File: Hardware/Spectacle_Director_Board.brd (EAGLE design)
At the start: 25.4 x 55.9 mm, 69 parts, among them J1 AUDIO-JACK3, J4 AUDIO-JACK3, Q2 MBT3904DW1T1, U1 CY7C65213, U2 ESP3212, U3 AP2112K-3.3V, U5 W25Q32FVSS, Y1 26MHz, Y2 32.768kHz

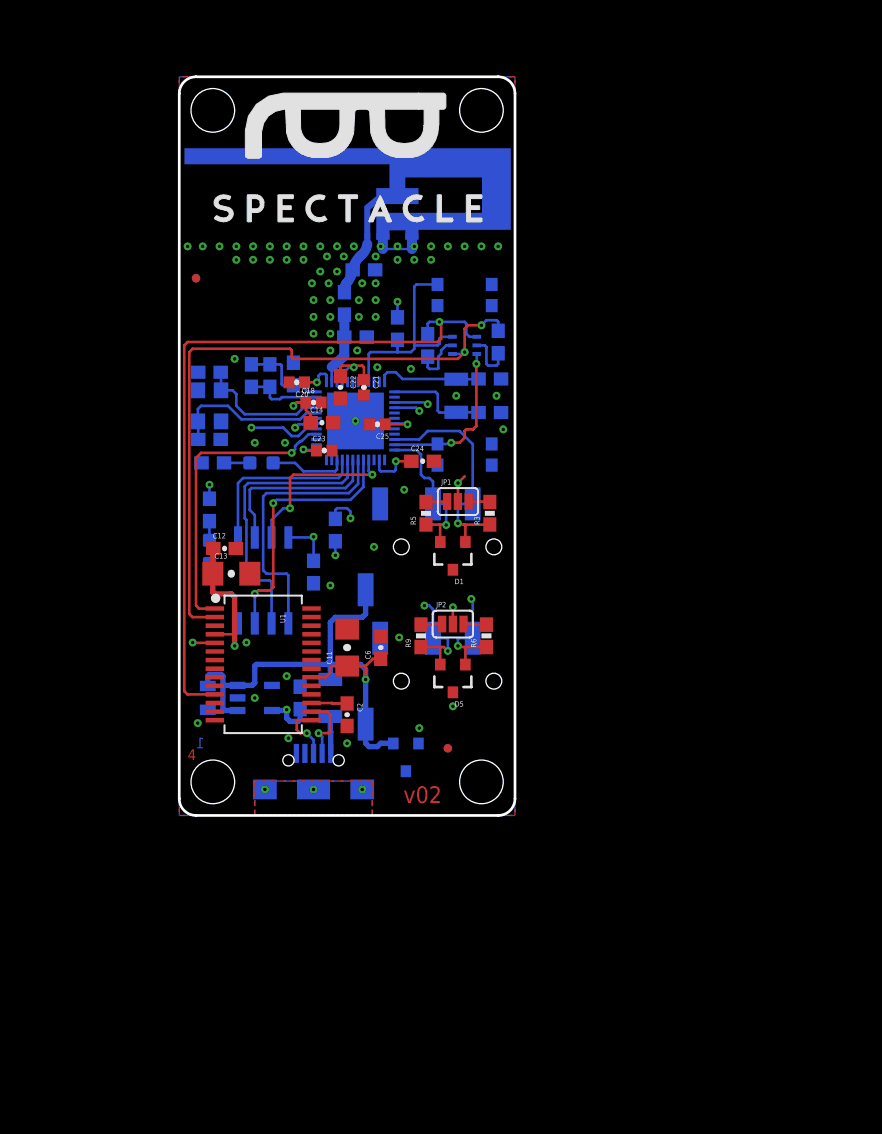
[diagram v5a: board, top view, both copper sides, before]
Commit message: Feedback from QC review incorporated
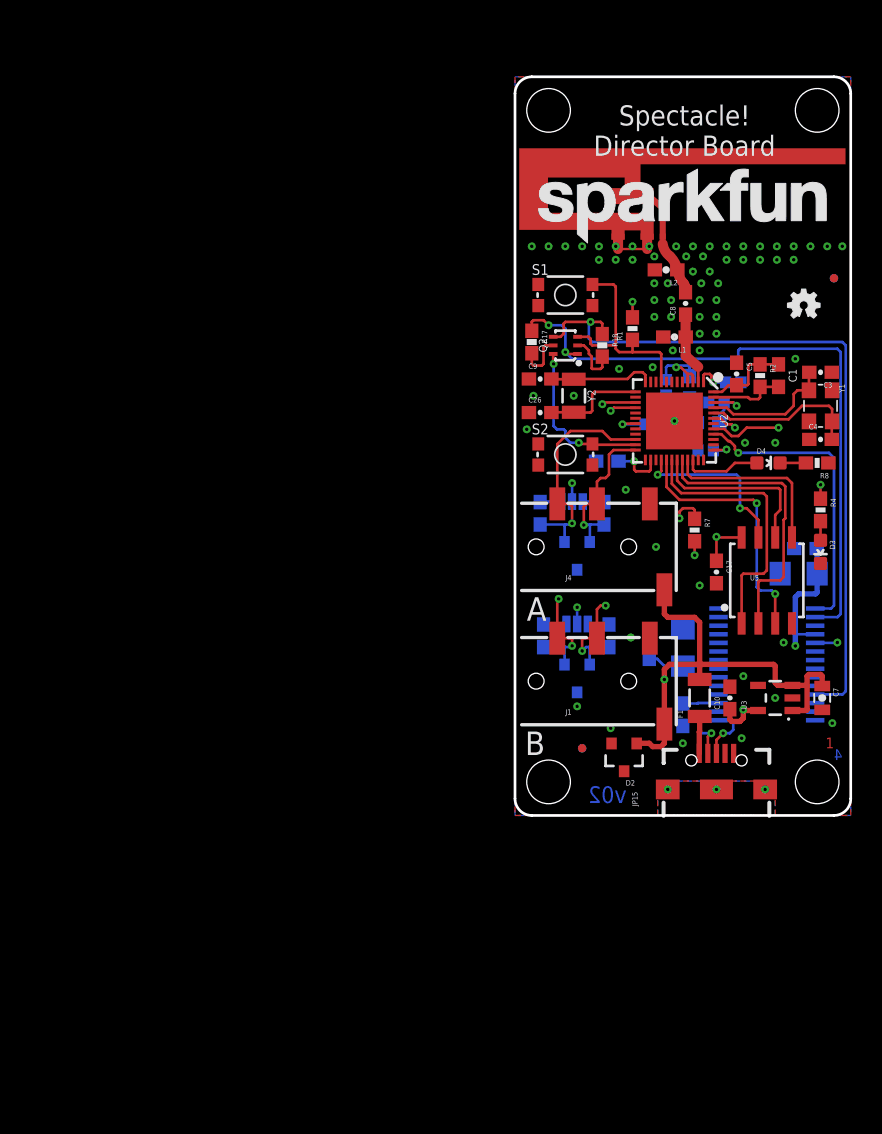
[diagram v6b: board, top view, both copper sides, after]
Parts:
- moved U$2 73.7 mm to (-36.8, -11.4), flipped to the top
- moved FD2 48.3 mm to (24.1, 40.6), flipped to the top
- moved FD4 48.3 mm to (24.1, 40.6), flipped to the bottom
- moved C7 46.5 mm to (23.2, 8.89), flipped to the top
- moved C3 46.2 mm to (23.1, 33.5), flipped to the top
- moved C4 46.2 mm to (23.1, 28.4), flipped to the top
- moved D3 46.2 mm to (23.1, 19.9), flipped to the top
- moved R4 46.2 mm to (23.1, 23.1), flipped to the top
- moved Y1 46.2 mm to (23.1, 31.0), flipped to the top
- moved H2 45.7 mm to (22.9, 53.3), flipped to the top
- moved H3 45.7 mm to (22.9, 2.54), flipped to the top
- moved R8 45.7 mm to (22.9, 26.7), flipped to the top
- moved C12 43.9 mm to (22.0, 20.2), flipped to the bottom
- moved LOGO2 43.7 mm to (21.8, 38.6), flipped to the top
- moved C13 42.9 mm to (21.5, 18.3), flipped to the bottom
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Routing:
- net 3.3V: track 44.9 -> 44.1 mm

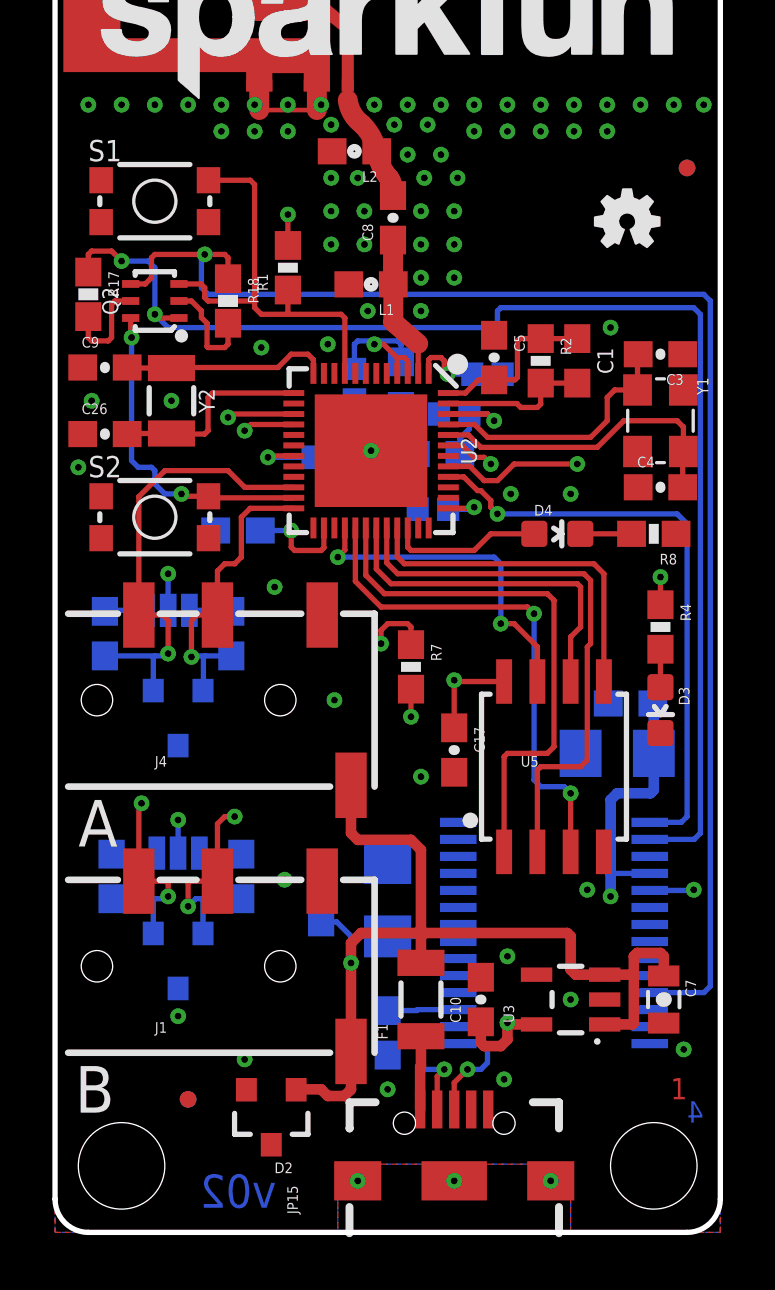
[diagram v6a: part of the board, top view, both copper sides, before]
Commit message: v03 - Removing RTC, I2C connector A, adding button, LED.
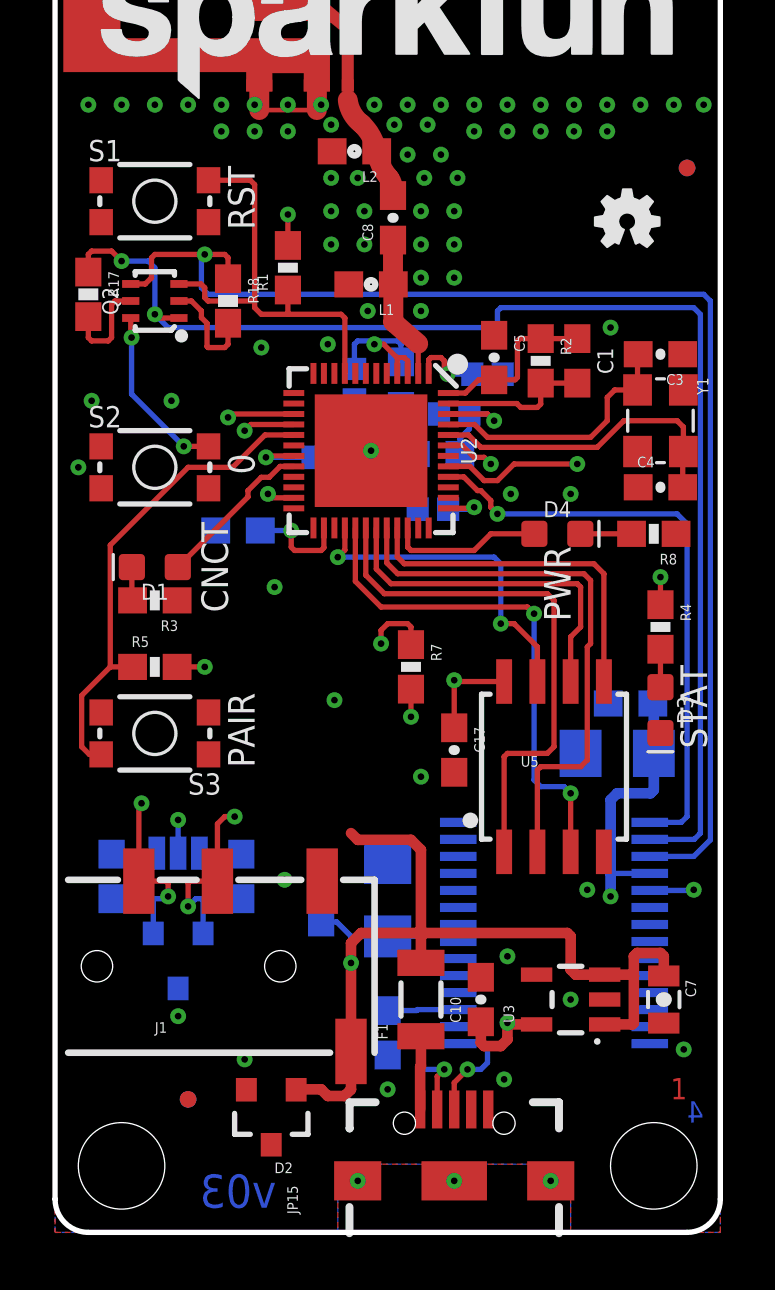
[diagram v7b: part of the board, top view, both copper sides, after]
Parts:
- removed C26, C9: 22pF, SparkFun-Capacitors:0603-CAP
- removed J4: AUDIO-JACK3, SparkFun-Connectors:AUDIO-JACK-TRRS-SMD
- removed JP1: JUMPER-PAD-3-NC_BY_PASTE, SparkFun-Passives:PAD-JUMPER-3-NC_BY_PASTE_YES_SILK_FULL_BOX
- removed Y2: 32.768kHz, SparkFun-Clocks:CRYSTAL-SMD-3.2X1.5MM
- added S3: BTN-14, SparkFun-Electromechanical:TACTILE_SWITCH_SMD_4.6X2.8MM
- D1: value PESD1CAN -> GREEN; device SparkFun-DiscreteSemi:SOT23-3 -> SparkFun-LED:LED-0603
- R3: value 2.2k -> 330
- R5: value 2.2k -> 10K
- moved D1 5.78 mm to (3.81, 25.4), flipped to the top
- moved R5 3.19 mm to (3.81, 21.6), flipped to the top, turned to 0 degrees
- moved R3 2.29 mm to (3.81, 24.1), flipped to the top, turned to 180 degrees
- moved S2 1.91 mm to (3.81, 29.2)
- turned D3 to 270 degrees
- turned D4 to 0 degrees
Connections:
- removed net GND18: U1.18
- removed net GND21: U1.21
- removed net GND7: U1.7
- removed net N$6: JP1.1, R5.2
- new net 13: D1.A, U2.20
- new net 14: R5.1, S3.3, U2.17
- net 3.3V: now also R5.2; no longer JP1.2
- net 32K_XN: no longer C26.2, Y2.P$2
- net 32K_XP: no longer C9.2, Y2.P$1
- net GND: now also R3.1, S3.1, U1.18, U1.21, U1.7; no longer C26.1, C9.1, D1.3, J4.TIP
- net I2C_SCL_1: no longer D1.1, J4.RING2, R3.1
- net I2C_SDA_1: no longer D1.2, J4.RING1, R5.1
- net N$3: now also D1.C; no longer JP1.3
- net RTS: now also U1.3; no longer U1.11
- net V_USB: no longer J4.EARTH
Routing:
- net 14: track 0.00 -> 18.6 mm
- net I2C_SCL_1: track 17.4 -> 0.00 mm, vias 1 -> 0
- net I2C_SDA_1: track 11.8 -> 0.00 mm, vias 1 -> 0
- net 32K_XP: track 7.95 -> 0.00 mm
- net 32K_XN: track 7.77 -> 0.00 mm
- net 13: track 0.00 -> 6.16 mm
- net RTS: track 55.0 -> 49.6 mm
- net 0: track 28.3 -> 24.1 mm, vias 3 -> 4
- net V_USB: track 42.1 -> 40.3 mm
- net N$6: track 1.62 -> 0.00 mm
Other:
- board text added: "0"
- board text added: "CNCT"
- board text added: "Mike Hord Jim Lindblom"
- board text added: "PAIR"
- board text added: "PWR"
- board text added: "RST"
- board text added: "STAT"
- board text added: "v03"
- board text removed: "A"
- board text removed: "B"
- board text removed: "Mike Hord"
- board text removed: "v02"

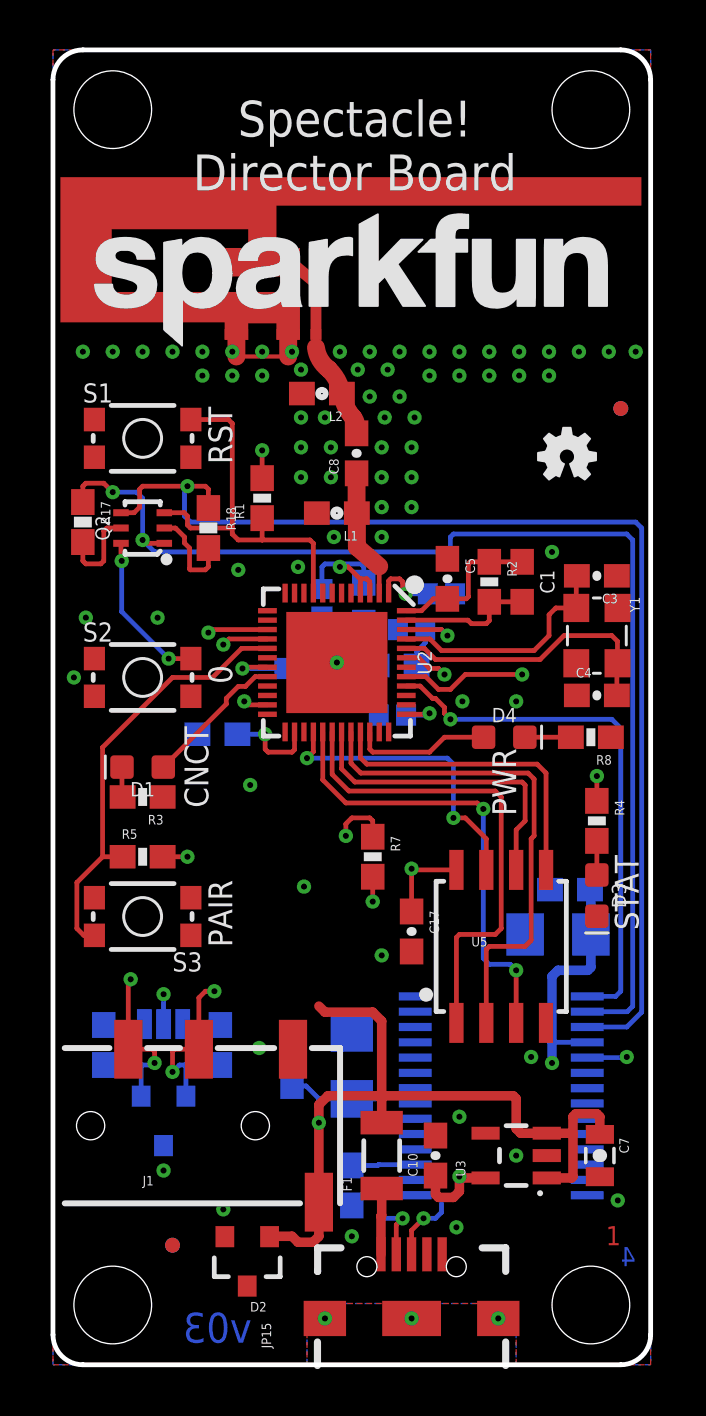
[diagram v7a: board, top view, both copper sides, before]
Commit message: initial commit of SAMD21-based director board.
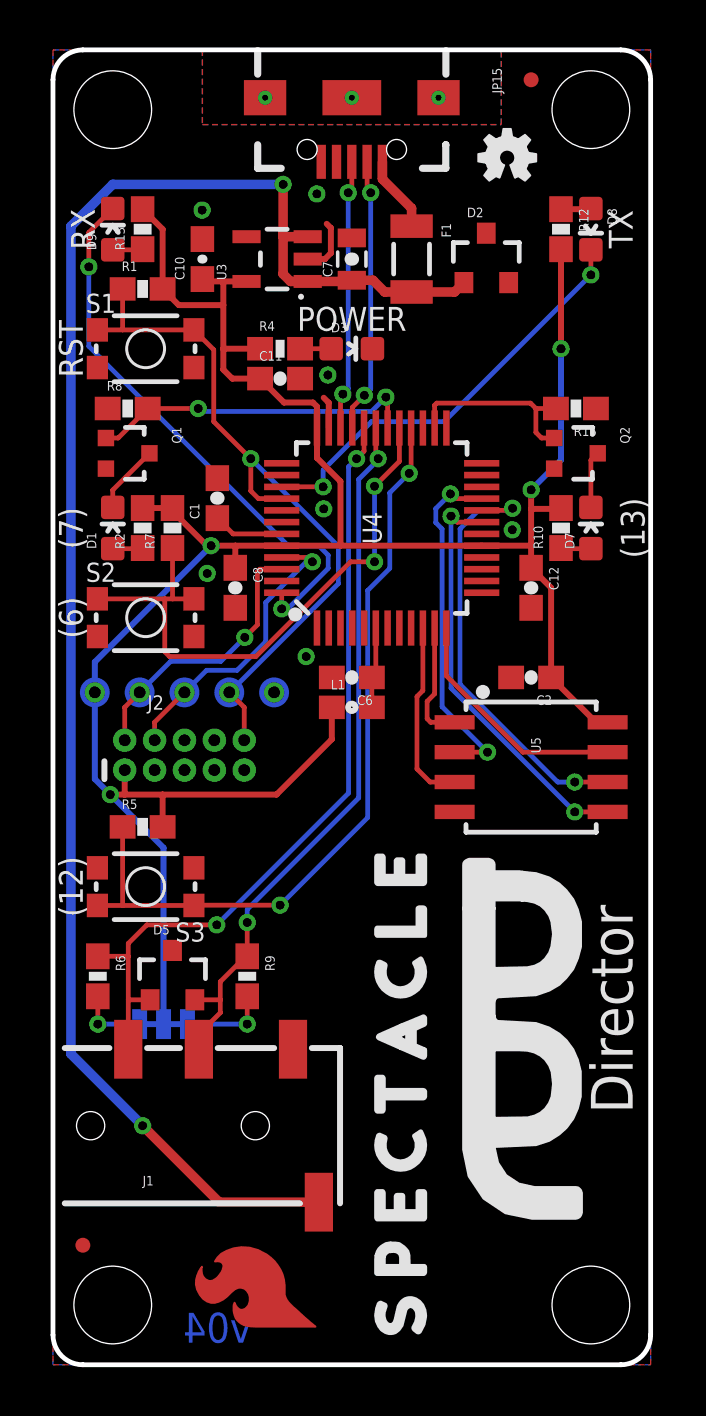
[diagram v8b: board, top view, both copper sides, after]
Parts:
- removed C13: 4.7uF, SparkFun-Capacitors:1206-CAP
- removed C14, C24: 1.0uF, SparkFun-Capacitors:0603-CAP
- removed C17: 0.1uF, SparkFun-Capacitors:0603-CAP
- removed C18, C20, C21, C23, C25: 0.1uF, SparkFun-Capacitors:0402-CAP
- removed C22: 10uF, SparkFun-Capacitors:0603-CAP
- removed C3, C4: 10pF, SparkFun-Capacitors:0603-CAP
- removed C5: 10nF, SparkFun-Capacitors:0603-CAP
- removed D4: BLUE, SparkFun-LED:LED-0603
- removed E1: ANTENNA, esp32-thing-temp:TRACE_ANTENNA_2.4GHZ_25.7MM_TUNED
- removed FD3, FD4: FIDUCIALUFIDUCIAL, SparkFun-Aesthetics:MICRO-FIDUCIAL
- removed FRAME1: FRAME-LEDGER, SparkFun-Aesthetics:CREATIVE_COMMONS
- removed L2: DNP, SparkFun-Passives:0603
- removed R17, R18: 10K, SparkFun-Resistors:0603-RES@1
- removed R3: 330, SparkFun-Resistors:0603-RES
- removed U$2: FOUR_LAYER_WARNING, SparkFun-Aesthetics:FOUR_LAYER_WARNING
- removed U1: CY7C65213, SparkFun-DigitalIC:SSOP28DB
- removed U2: ESP3212, esp32-thing-temp:QFN48-0.4MM
- removed Y1: 26MHz, things:CRYSTAL-SMD-3.2X2.5
- added D7: BLUE, SparkFun-LED:LED-0603
- added D8: GREEN, SparkFun-LED:LED-0603
- added D9: Yellow, SparkFun-LED:LED-0603
- added FRAME2: FRAME-LETTER, SparkFun-Aesthetics:CREATIVE_COMMONS
- added J2: CORTEX_DEBUGPTH, SparkFun-Connectors:2X5-PTH-1.27MM
- added LOGO3: SFE_LOGO_FLAME.2EXP, SparkFun-Aesthetics:SFE_LOGO_FLAME_COPPER_EXPOSED_.2
- added Q1: 2N7002PW, SparkFun-DiscreteSemi:SOT323
- added R10, R12, R13: 330, SparkFun-Resistors:0603-RES
- added R15: 100k, SparkFun-Resistors:0603-RES
- added TP1, TP2, TP3, TP4, TP5: TEST-POINT3X5, SparkFun-Connectors:PAD.03X.05
- added U$1: (no value), SparkFun-Aesthetics:ORDERING_INSTRUCTIONS
- added U4: ATSAMD21G-A, samd21-temp:TQFP-48
- C1: value 3.0nF -> 0.1uF; device esp32-thing-temp:0603 -> SparkFun-Capacitors:0603-CAP
- C10: device SparkFun-Capacitors:0603-CAP -> SparkFun-Capacitors:0603-CAP@1
- C11: value 4.7uF -> 0.1uF; device SparkFun-Capacitors:1206-CAP -> SparkFun-Capacitors:0603-CAP
- C2: value 1.0uF -> 0.1uF
- C8: value 5.6pF -> 0.1uF
- JP2: value JUMPER-PAD-3-NC_BY_PASTE -> JUMPER-SMT_3_2-NC_TRACE_SILK; device SparkFun-Passives:PAD-JUMPER-3-NC_BY_PASTE_YES_SILK_FULL_BOX -> SparkFun-Jumpers:SMT-JUMPER_3_2-NC_TRACE_SILK
- L1: value DNP -> FB - 30Ohm
- Q2: value MBT3904DW1T1 -> 2N7002PW; device esp32-thing-temp:SC70-6 -> SparkFun-DiscreteSemi:SOT323
- R2: value 20k -> 330
- R4, R6, R9: device SparkFun-Resistors:0603-RES -> SparkFun-Resistors:0603-RES@1
- R8: value 330 -> 100k
- S2: value BTN-0 -> BTN2
- S3: value BTN-14 -> BTN1
- moved JP15 51.9 mm to (12.7, 53.8), turned to 270 degrees
- moved D2 43.7 mm to (18.4, 47.0), turned to 0 degrees
- moved C7 39.5 mm to (12.7, 47.0), turned to 90 degrees
- moved U3 39.4 mm to (9.53, 47.0)
- moved C10 39.4 mm to (6.35, 47.0)
- moved F1 38.1 mm to (15.2, 47.0), turned to 270 degrees
- moved C11 29.4 mm to (9.65, 41.9), flipped to the top, turned to 0 degrees
- moved D3 25.5 mm to (12.7, 43.2)
- moved R4 24.2 mm to (9.65, 43.2), turned to 0 degrees
- moved R8 24.1 mm to (3.17, 40.6), turned to 0 degrees
- moved C2 22.9 mm to (20.3, 29.2), flipped to the top, turned to 180 degrees
- moved LOGO1 21.9 mm to (23.6, 44.6), flipped to the bottom
- moved Q2 18.7 mm to (22.2, 38.7), turned to 270 degrees
- moved C6 16.7 mm to (12.7, 29.2), flipped to the top, turned to 180 degrees
- moved R7 16.4 mm to (5.08, 35.6), turned to 90 degrees
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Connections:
- removed net 0: Q2.6, R7.1, S2.3, U2.23
- removed net 13: D1.A, U2.20
- removed net 14: R5.1, S3.3, U2.17
- removed net 32K_XN: U2.13
- removed net 32K_XP: U2.12
- removed net 5: D4.A, U2.34
- removed net CAP_10N: C1.1, C5.2, R2.1, U2.48
- removed net CHIP_PU: Q2.3, R1.1, S1.3, U2.9
- removed net DTR: Q2.1, R17.1, U1.2
- removed net FLASH_SCK: U2.31, U5.6
- removed net FLASH_SCS: U2.30, U5.1
- removed net FLASH_SDI: U2.33, U5.5
- removed net FLASH_SDO: U2.32, U5.2
- removed net FLASH_SHD: U2.28, U5.7
- removed net FLASH_SWP: U2.29, U5.3
- removed net FLASH_VDD: C24.1, U2.26
- removed net I2C_SCL_0: D5.1, J1.RING2, R6.1, U2.15
- removed net I2C_SCL_1: U2.22
- removed net I2C_SDA_0: D5.2, J1.RING1, R9.1, U2.16
- removed net I2C_SDA_1: U2.24
- removed net LNA_IN: C8.1, L1.1, U2.2
- removed net N$3: D1.C, R3.2
- removed net N$8: JP15.D+, U1.15
- removed net NC1: U1.25
- removed net RTS: Q2.4, R18.1, U1.3
- removed net TRACE_ANT: C8.2, E1.ANT, L2.1
- removed net U0RXD: U1.1, U2.40
- removed net U0TXD: U1.5, U2.41
- removed net VDD: C2.1, U1.17
- removed net XTAL_N_: C4.2, U2.44, Y1.3
- removed net XTAL_P_: C3.2, U2.45, Y1.1
- new net !RESET: J2.10, R1.1, S1.3, S1.4, TP3.P$1, U4.40
- new net A0: U4.3
- new net A1: U4.7
- new net A2: U4.8
- new net A3: U4.9
- new net A4_FLASH!WP!: U4.10, U5.3
- new net A5: U4.47
- new net AREF: U4.4
- new net D10: U4.27
- new net D11: U4.25
- new net D12_BTN1: R5.1, S3.3, S3.4, U4.28
- new net D13_LED1: Q2.1, R15.2, U4.26
- new net D2: U4.23
- new net D5: U4.24
- new net D6_BTN2: R7.1, S2.3, S2.4, U4.29
- new net D7_LED2: Q1.1, R8.2, U4.30
- new net D8_FLASH!CS!: U4.11, U5.1
- new net D9_FLASH!HD!: U4.12, U5.7
- new net N$9: D7.A, R10.1
- new net PB22: U4.37
- new net PB23: U4.38
- new net RX_LED: D9.C, U4.48
- new net SCL: D5.1, J1.RING2, R6.1, U4.32
- new net SDA: D5.2, J1.RING1, R9.1, U4.31
- new net SPI_MISO: U4.21, U5.2
- new net SPI_MOSI: U4.19, U5.5
- new net SPI_SCK: U4.20, U5.6
- new net SWCLK: J2.4, TP2.P$1, U4.45
- new net SWDIO: J2.2, TP1.P$1, U4.46
- new net TX_LED: D8.C, U4.39
- new net USB_D+: JP15.D+, U4.34
- new net USB_D-: JP15.D-, U4.33
- new net USB_HOST_EN: U4.41
- new net VDDANA: C6.1, L1.2, U4.6
- new net VDDCORE: C1.1, U4.43
- net 3.3V: now also C11.1, C2.1, C8.1, J2.1, L1.1, R10.2, R12.2, R13.2, R2.2, TP4.P$1, U4.17, U4.36, U4.44; no longer C13.1, C14.1, C17.1, C18.1, C20.1, C21.1, C22.1, C23.1, C25.1, U1.4, U2.1, U2.19, U2.3, U2.37, U2.4, U2.43, U2.46
- net GND: now also C1.2, C8.2, J2.3, J2.5, Q1.2, Q2.2, R15.1, S1.2, S2.2, S3.2, TP5.P$1, U4.18, U4.35, U4.42, U4.5; no longer C13.2, C14.2, C17.2, C18.2, C20.2, C21.2, C22.2, C23.2, C24.2, C25.2, C3.1, C4.1, C5.1, E1.GND, E1.GND2, L1.2, L2.2, R3.1, U1.18, U1.21, U1.7, U2.EP, Y1.2, Y1.4
- net N$1: now also D1.A, R2.1; no longer D4.C, R8.2
- net N$10: now also D7.C, Q2.3; no longer Q2.5, R17.2
- net N$11: now also D8.A, R12.1; no longer C1.2, R2.2, U2.47
- net N$12: now also D9.A, R13.1; no longer Q2.2, R18.2
- net N$7: now also D1.C, Q1.3; no longer JP15.D-, U1.16
- net V_USB: no longer C11.1, C6.1, U1.20
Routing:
- net 3.3V: track 43.8 -> 104.5 mm, vias 14 -> 5
- net DTR: track 49.9 -> 0.00 mm, vias 2 -> 0
- net RTS: track 49.6 -> 0.00 mm, vias 1 -> 0
- net SCL: track 0.00 -> 34.5 mm, vias 0 -> 2
- net D12_BTN1: track 0.00 -> 33.7 mm, vias 0 -> 2
- net V_USB: track 40.3 -> 71.5 mm, vias 1 -> 2
- net !RESET: track 0.00 -> 30.8 mm, vias 0 -> 2
- net SDA: track 0.00 -> 30.7 mm, vias 0 -> 2
- net I2C_SCL_0: track 28.7 -> 0.00 mm, vias 3 -> 0
- net U0TXD: track 27.7 -> 0.00 mm, vias 2 -> 0
- net D6_BTN2: track 0.00 -> 25.5 mm, vias 0 -> 2
- net I2C_SDA_0: track 25.4 -> 0.00 mm, vias 3 -> 0
- net 0: track 24.1 -> 0.00 mm, vias 4 -> 0
- net RX_LED: track 0.00 -> 24.1 mm, vias 0 -> 2
- net U0RXD: track 22.7 -> 0.00 mm, vias 1 -> 0
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- removed copper zone on layer 15, net 3.3V
- removed copper zone on layer 2, net GND
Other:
- board text added: "(12)"
- board text added: "(13)"
- board text added: "(6)"
- board text added: "(7)"
- board text added: "Director"
- board text added: "POWER"
- board text added: "RX"
- board text added: "TX"
- board text added: "v04"
- board text removed: "0"
- board text removed: "1"
- board text removed: "2"
- board text removed: "3"
- board text removed: "4"
- board text removed: "CNCT"
- board text removed: "PAIR"
- board text removed: "PWR"
- board text removed: "STAT"
- board text removed: "v03"
